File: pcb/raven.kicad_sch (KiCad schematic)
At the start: 43 parts, among them J1 Conn_02x20_Odd_Even, J2 Conn_01x04_MountingPin, J3 Conn_01x02_Pin, J4 Conn_01x02_Pin, J5 Conn_01x04_MountingPin, J6 Conn_01x02_Pin, J7 Conn_01x02_Pin, J8 Conn_01x02_Pin, J9 Conn_01x02_Pin, U9 TPS548B28RWWR

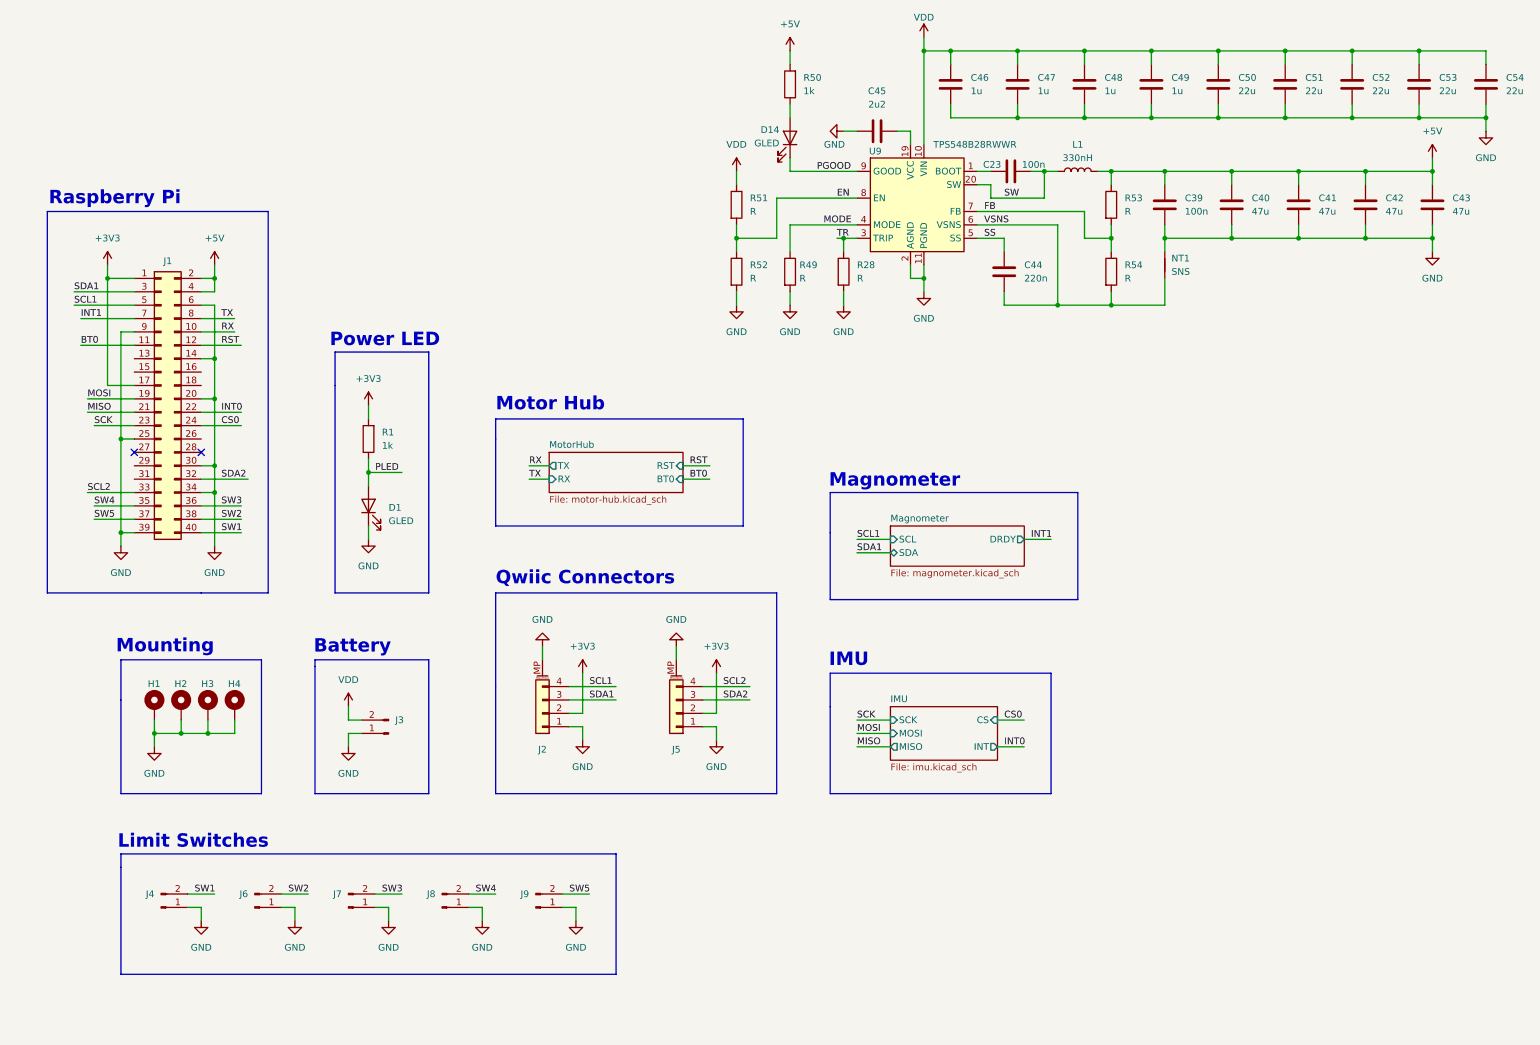
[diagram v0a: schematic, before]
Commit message: Finish schematic
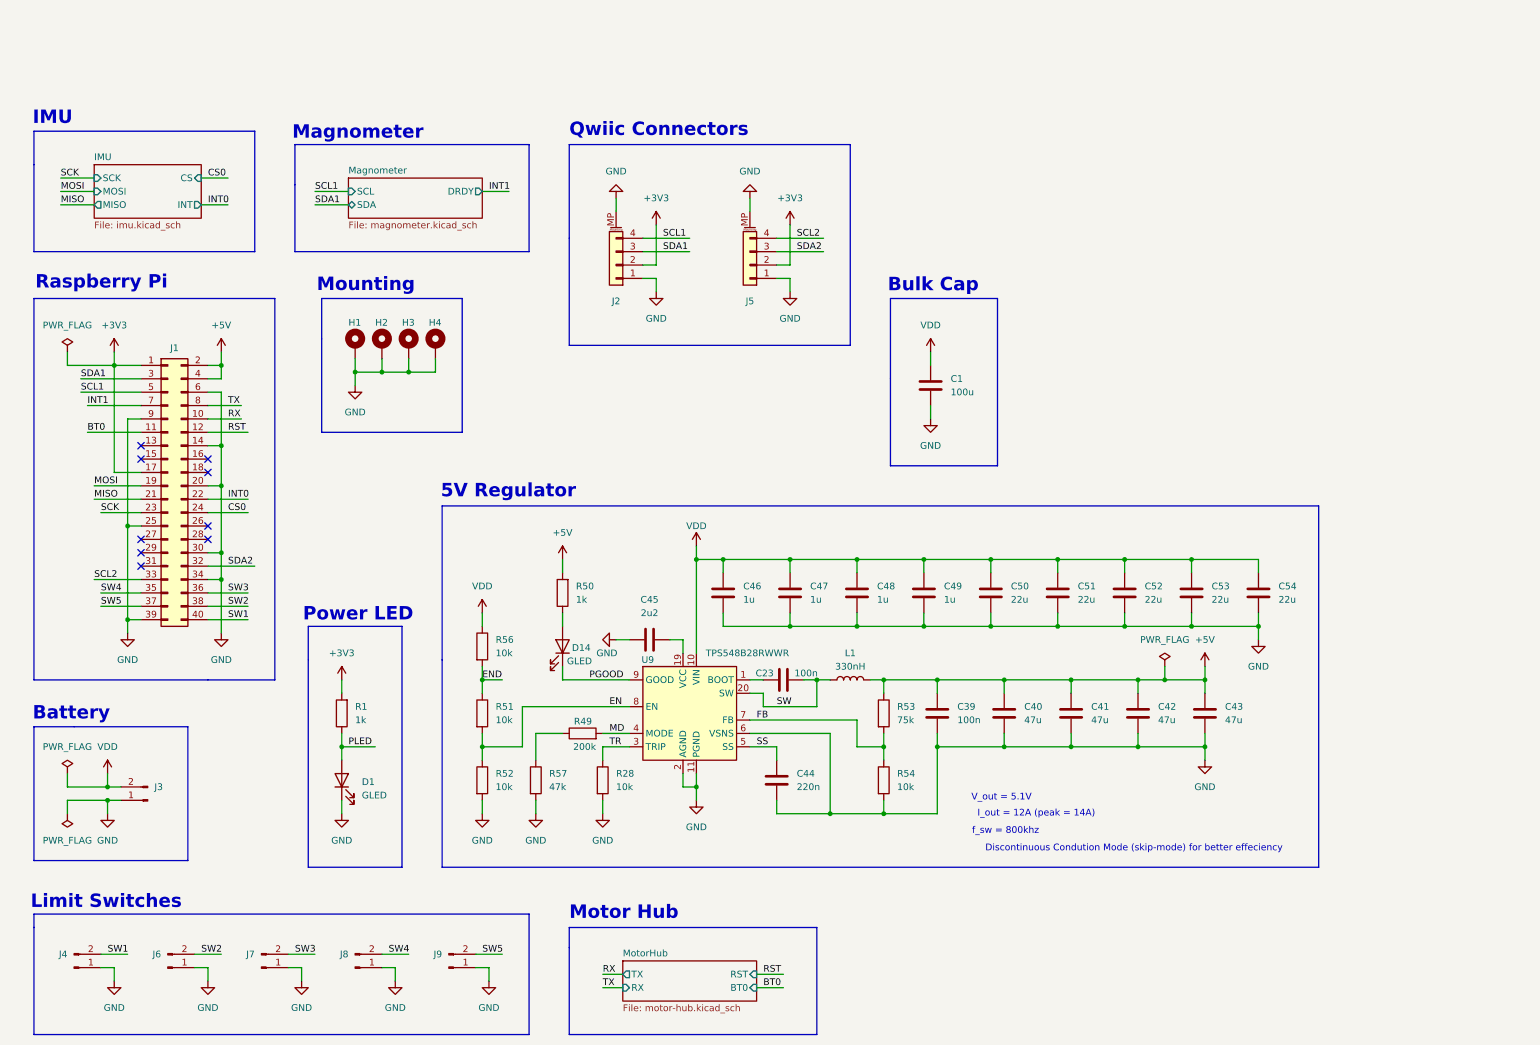
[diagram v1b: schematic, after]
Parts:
- removed NT1: SNS, symbol Device:NetTie_2
- added C1: 100u, Capacitor_SMD:C_Elec_8x6.2, symbol Device:C
- added R56: 10k, Resistor_SMD:R_0402_1005Metric, symbol Device:R
- added R57: 47k, Resistor_SMD:R_0402_1005Metric, symbol Device:R
- C23: LCSC (none) -> C14663
- C44: footprint Capacitor_SMD:C_0603_1608Metric -> Capacitor_SMD:C_0402_1005Metric
- J1: footprint Connector_PinHeader_2.54mm:PinHeader_2x20_P2.54mm_Vertical -> Connector_PinSocket_2.54mm:PinSocket_2x20_P2.54mm_Vertical; LCSC (none) -> C35165
- J3: LCSC (none) -> C431092
- J4, J6, J7, J8, J9: LCSC (none) -> C492401
- R28, R51, R52, R54: value R -> 10k; LCSC (none) -> C25744
- R49: value R -> 200k; LCSC (none) -> C25764
- R53: value R -> 75k; LCSC (none) -> C25798
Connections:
- net VSNS is gone; now on net GND: C44.2, R54.2, U9.6 (VSNS)
- net GND: now also C1.2, R57.2; no longer R49.2
- net VDD: now also C1.1, R56.1; no longer R51.1
- net MODE: no longer names the net of R49.1
- net MODE: now also R57.1; no longer U9.4 (MODE)
- new net END: R51.1, R56.2
- new net MD: R49.2, U9.4 (MODE)
- no-connect marks 2 -> 9
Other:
- note added: "5V Regulator"
- note added: "Bulk Cap"
- note added: "Discontinuous Condution Mode (skip-mode) for better effeciency"
- note added: "I_out = 12A (peak = 14A)"
- note added: "V_out = 5.1V"
- note added: "f_sw = 800khz"
- moved on the sheet: C23, C39, C40, C41, C42, C43, C44, C45, C46, C47, C48, C49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

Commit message: Save progress
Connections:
- net SW1: now also J1.31 (Pin_31); no longer J1.40 (Pin_40)
- net SW2: now also J1.36 (Pin_36); no longer J1.38 (Pin_38)
- net SW3: now also J1.29 (Pin_29); no longer J1.36 (Pin_36)
- net SW4: now also J1.26 (Pin_26); no longer J1.35 (Pin_35)
- net SW5: now also J1.35 (Pin_35); no longer J1.37 (Pin_37)
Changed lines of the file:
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@@
 	)
 	(no_connect
-		(at 39.37 100.33)
+		(at 52.07 113.03)
 	)
 	(no_connect
@@
 	)
 	(no_connect
-		(at 52.07 95.25)
+		(at 52.07 110.49)
 	)
 	(no_connect
@@
 	)
 	(no_connect
-		(at 39.37 102.87)
+		(at 39.37 110.49)
 	)
 	(wire
@@
 	(wire
 		(pts
+			(xy 31.75 100.33) (xy 39.37 100.33)
+		)
+		(stroke
+			(width 0)
+			(type default)
+		)
+	)
+	(wire
+		(pts
 			(xy 127 182.88) (xy 130.81 182.88)
 		)
@@
 	(wire
 		(pts
-			(xy 52.07 110.49) (xy 59.69 110.49)
+			(xy 52.07 107.95) (xy 59.69 107.95)
 		)
 		(stroke
@@
 	(wire
 		(pts
-			(xy 52.07 107.95) (xy 59.69 107.95)
-		)
-		(stroke
-			(width 0)
-			(type default)
-		)
-	)
-	(wire
-		(pts
 			(xy 251.46 101.6) (xy 251.46 104.14)
 		)
@@
 	(wire
 		(pts
-			(xy 31.75 110.49) (xy 39.37 110.49)
+			(xy 31.75 107.95) (xy 39.37 107.95)
 		)
 		(stroke
@@
 	(wire
 		(pts
+			(xy 31.75 102.87) (xy 39.37 102.87)
+		)
+		(stroke
+			(width 0)
+			(type default)
+		)
+	)
+	(wire
+		(pts
+			(xy 52.07 95.25) (xy 59.69 95.25)
+		)
+		(stroke
+			(width 0)
+			(type default)
+		)
+	)
+	(wire
+		(pts
 			(xy 69.85 179.07) (xy 67.31 179.07)
 		)
@@
 		)
 	)
-	(wire
-		(pts
-			(xy 31.75 107.95) (xy 39.37 107.95)
-		)
-		(stroke
-			(width 0)
-			(type default)
-		)
-	)
 	(polyline
 		(pts
@@
 		)
 	)
-	(wire
-		(pts
-			(xy 52.07 113.03) (xy 59.69 113.03)
-		)
-		(stroke
-			(width 0)
-			(type default)
-		)
-	)
 	(text "Mounting"
 		(exclude_from_sim no)
@@
 	)
 	(label "SW3"
-		(at 55.88 107.95 0)
-		(fields_autoplaced yes)
-		(effects
-			(font
-				(size 1.27 1.27)
-			)
-			(justify left bottom)
-		)
-	)
-	(label "SW3"
 		(at 68.58 176.53 0)
 		(fields_autoplaced yes)
@@
 	)
 	(label "SW5"
-		(at 31.75 110.49 0)
+		(at 31.75 107.95 0)
 		(fields_autoplaced yes)
 		(effects
@@
 	)
 	(label "SW2"
-		(at 55.88 110.49 0)
+		(at 55.88 107.95 0)
 		(fields_autoplaced yes)
 		(effects
@@
 		)
 	)
+	(label "SW3"
+		(at 31.75 100.33 0)
+		(fields_autoplaced yes)
+		(effects
+			(font
+				(size 1.27 1.27)
+			)
+			(justify left bottom)
+		)
+	)
 	(label "END"
 		(at 104.14 124.46 0)
@@
 		)
 	)
+	(label "SW1"
+		(at 31.75 102.87 0)
+		(fields_autoplaced yes)
+		(effects
+			(font
+				(size 1.27 1.27)
+			)
+			(justify left bottom)
+		)
+	)
 	(label "MOSI"
 		(at 24.13 31.75 0)
@@
 		)
 	)
-	(label "SW4"
-		(at 31.75 107.95 0)
-		(fields_autoplaced yes)
-		(effects
-			(font
-				(size 1.27 1.27)
-			)
-			(justify left bottom)
-		)
-	)
 	(label "INT1"
 		(at 29.21 72.39 0)
@@
 		)
 	)
-	(label "MD"
-		(at 128.27 134.62 0)
+	(label "SW4"
+		(at 55.88 95.25 0)
 		(fields_autoplaced yes)
 		(effects
@@
 		)
 	)
-	(label "SW1"
-		(at 55.88 113.03 0)
+	(label "MD"
+		(at 128.27 134.62 0)
 		(fields_autoplaced yes)
 		(effects

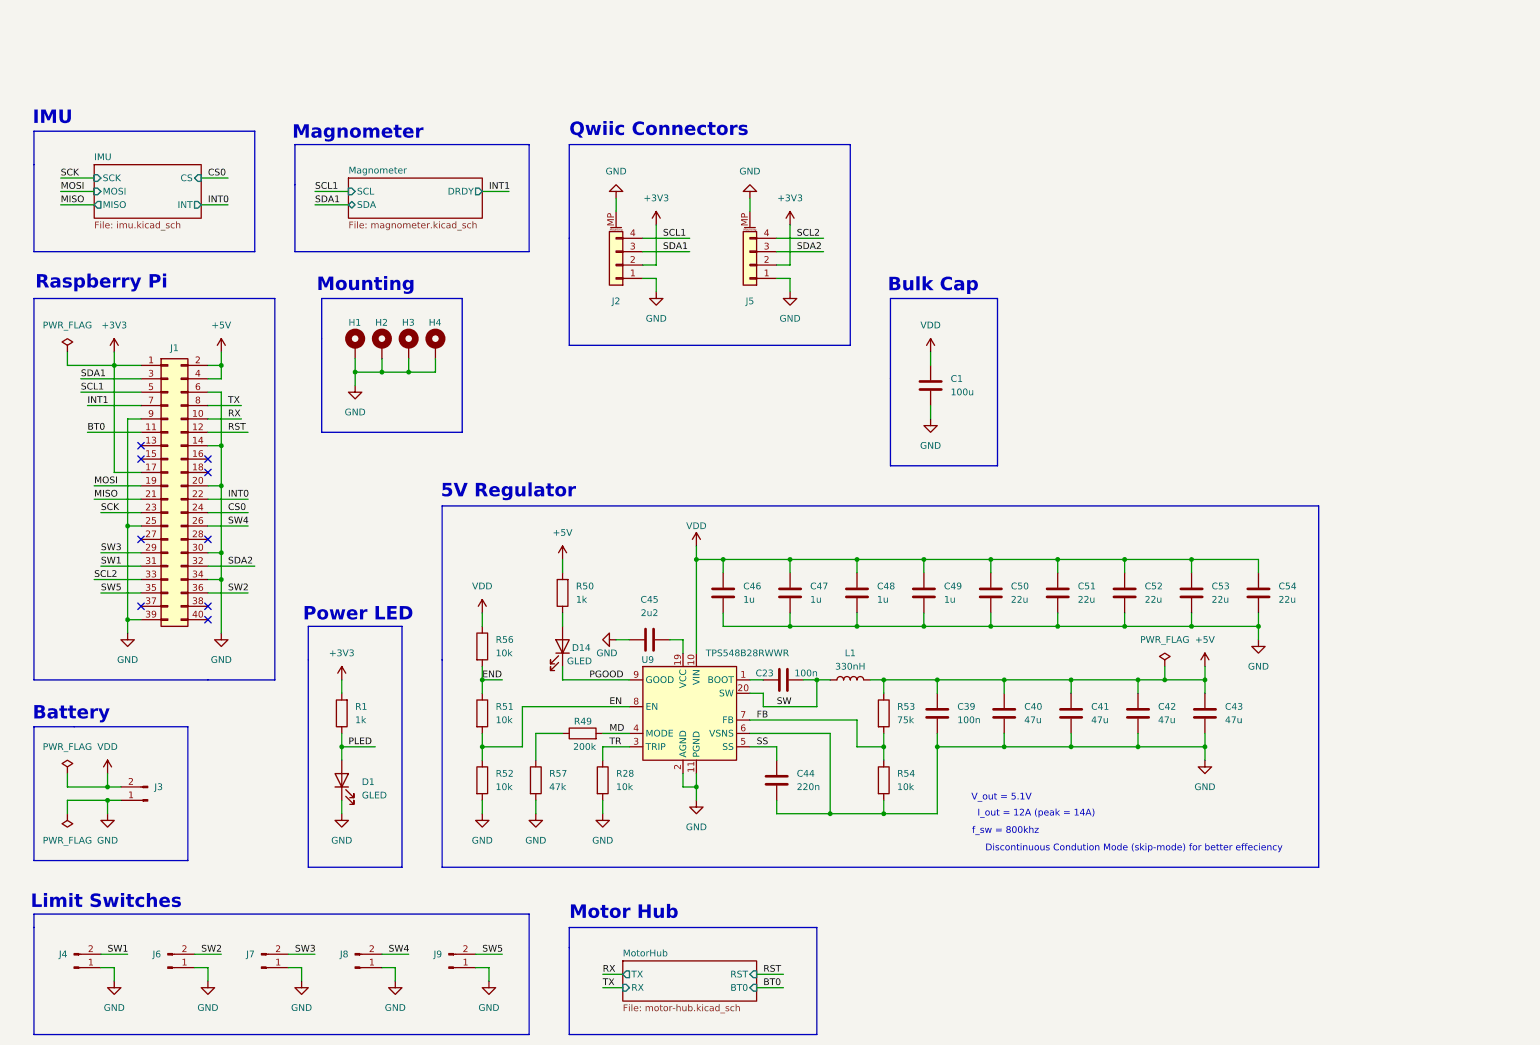
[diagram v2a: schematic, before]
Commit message: Finish lipo shutdown
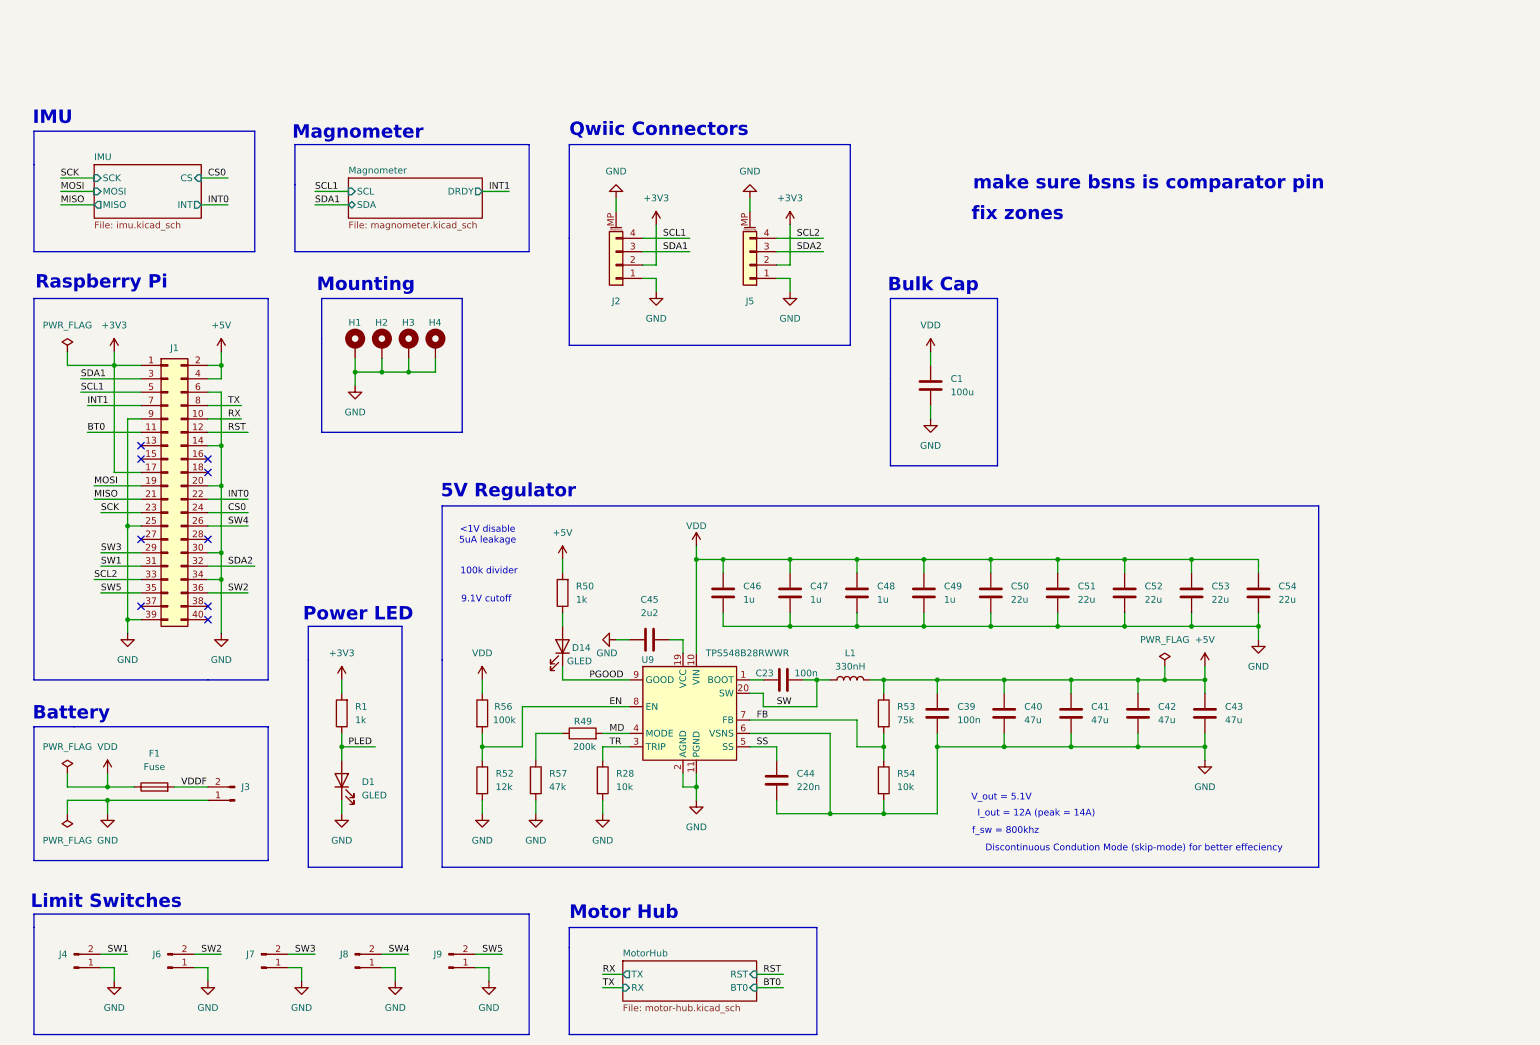
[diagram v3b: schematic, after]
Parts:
- removed R51: 10k, Resistor_SMD:R_0402_1005Metric, symbol Device:R
- added F1: Fuse, Fuse:Fuse_1206_3216Metric, symbol Device:Fuse
- J3: footprint Connector_AMASS:AMASS_XT30PW-M_1x02_P2.50mm_Horizontal -> Connector_AMASS:AMASS_XT30UPB-M_1x02_P5.0mm_Vertical; LCSC C431092 -> C428721
- R52: value 10k -> 12k; LCSC C25744 -> C25752
- R56: value 10k -> 100k; LCSC C25744 -> C25741
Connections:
- net END is gone; now on net EN: R56.2
- net VDD: now also F1.1; no longer J3.2 (Pin_2)
- new net VDDF: F1.2, J3.2 (Pin_2)
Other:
- note added: "100k divider"
- note added: "9.1V cutoff"
- note added: "<1V disable 5uA leakage"
- note added: "fix zones"
- note added: "make sure bsns is comparator pin"
- moved on the sheet: J3, R56

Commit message: Finish routing
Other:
- note removed: "fix zones"
- note removed: "make sure bsns is comparator pin"
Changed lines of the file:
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@@
-		)
-	)
-	(text "fix zones"
-		(exclude_from_sim no)
-		(at 205.74 36.068 0)
-		(effects
-			(font
-				(size 2.54 2.54)
-				(thickness 0.508)
-				(bold yes)
-			)
 		)
 	)
@@
 		)
 	)
-	(text "make sure bsns is comparator pin"
-		(exclude_from_sim no)
-		(at 230.632 30.226 0)
-		(effects
-			(font
-				(size 2.54 2.54)
-				(thickness 0.508)
-				(bold yes)
-			)
-		)
-	)
